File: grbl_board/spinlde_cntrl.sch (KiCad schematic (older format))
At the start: 11 parts

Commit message: spindle control stage
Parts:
- removed C?: 100n, symbol Device:C
- removed U?: LMV321, symbol Amplifier_Operational:LMV321
- added C? (x2): 100n, symbol Device:C
- added C? (x2): 220p, symbol Device:C
- added C?: 10u, symbol Device:C
- added C?: 6.8n, symbol Device:C
- added C?: 100u, symbol Device:C
- added D? (x2): 1N4148, Diode_THT:D_DO-35_SOD27_P7.62mm_Horizontal, symbol Diode:1N4148
- added D?: SS2150-LTP, symbol Device:D_Schottky
- added D? (x2): BZX84Cxx, Diode_SMD:D_SOT-23_ANK, symbol Diode:BZX84Cxx
- added J?: freq, symbol Connector:Screw_Terminal_01x02
- added J?: Spindle, symbol Connector:Screw_Terminal_01x02
- added L?: 33u, symbol Device:L
- added Q?: NDS7002A, symbol Device:Q_NMOS_GSD
- added Q?: Q_PMOS_GDS, symbol Device:Q_PMOS_GDS
- added Q? (x2): BSS127S, Package_TO_SOT_SMD:SOT-23, symbol Transistor_FET:BSS127S
- added R? (x2): 100, symbol Device:R
- added R? (x5): 10k, symbol Device:R
- added R?: 250, symbol Device:R
- added R?: 22, symbol Device:R
- added R? (x2): 5k, symbol Device:R
- added R? (x3): 4k, symbol Device:R
- added R?: 1k, symbol Device:R
- added R? (x3): 500, symbol Device:R
- added R? (x2): 1, symbol Device:R
- added R?: 47k, symbol Device:R
- added R?: 2.2k, symbol Device:R
- added R?: 200, symbol Device:R
- added U?: L7805, symbol Regulator_Linear:L7805
- added U?: OPA2192, symbol grbl_board:OPA2192
- added U? (x3): LMV358, symbol Amplifier_Operational:LMV358
- added U?: BD9G341EFJ, Package_SO:HTSOP-8-1EP_3.9x4.9mm_P1.27mm_EP2.4x3.2mm_ThermalVias, symbol Regulator_Switching:BD9G341EFJ
- added U? (x2): 6N137, Package_DIP:DIP-8_W7.62mm, symbol Isolator:6N137
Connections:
- net labels added: 12V, 1V_REF, 24V_VFD, GND_VFD, SPINDLE_DIR, SPINDLE_EN
- wire segments 32 -> 203
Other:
- moved on the sheet: C?, J?, R?, U?

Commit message: changed to matched resistor
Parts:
- removed R? (x2): 10k, symbol Device:R
- added RN? (x2): LT5400_10k, symbol Device:R_Pack04_Split
- Q?: value Q_PMOS_GDS -> IRF9Z24S
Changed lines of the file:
@@
 P 9350 4950
 F 0 "Q?" H 9555 4996 50  0000 L CNN
-F 1 "Q_PMOS_GDS" H 9555 4905 50  0000 L CNN
+F 1 "IRF9Z24S" H 9555 4905 50  0000 L CNN
 F 2 "" H 9550 5050 50  0001 C CNN
 F 3 "~" H 9350 4950 50  0001 C CNN
@@
 Wire Wire Line
 	7550 3050 7550 3150
-$Comp
-L Device:R R?
-U 1 1 62254479
-P 7550 2900
-F 0 "R?" H 7620 2946 50  0000 L CNN
-F 1 "10k" H 7620 2855 50  0000 L CNN
-F 2 "" V 7480 2900 50  0001 C CNN
-F 3 "~" H 7550 2900 50  0001 C CNN
-	1    7550 2900
-	1    0    0    -1
-$EndComp
 Wire Wire Line
 	8050 2650 8050 2700
@@
 Wire Wire Line
 	9450 4450 9450 4550
-$Comp
-L Device:R R?
-U 1 1 622497C7
-P 9450 4300
-F 0 "R?" H 9520 4346 50  0000 L CNN
-F 1 "10k" H 9520 4255 50  0000 L CNN
-F 2 "" V 9380 4300 50  0001 C CNN
-F 3 "~" H 9450 4300 50  0001 C CNN
-	1    9450 4300
-	1    0    0    -1
-$EndComp
 Wire Wire Line
 	9100 3800 9150 3800
@@
 Wire Wire Line
 	2300 6750 2950 6750
+$Comp
+L Device:R_Pack04_Split RN?
+U 1 1 6182439D
+P 9450 4300
+F 0 "RN?" H 9538 4346 50  0000 L CNN
+F 1 "LT5400_10k" H 9538 4255 50  0000 L CNN
+F 2 "" V 9370 4300 50  0001 C CNN
+F 3 "~" H 9450 4300 50  0001 C CNN
+	1    9450 4300
+	1    0    0    -1
+$EndComp
+$Comp
+L Device:R_Pack04_Split RN?
+U 2 1 61833B71
+P 7550 2900
+F 0 "RN?" H 7638 2946 50  0000 L CNN
+F 1 "LT5400_10k" H 7638 2855 50  0000 L CNN
+F 2 "" V 7470 2900 50  0001 C CNN
+F 3 "~" H 7550 2900 50  0001 C CNN
+	2    7550 2900
+	1    0    0    -1
+$EndComp
 $EndSCHEMATC

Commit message: added some footprint associations
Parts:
- removed Q?: NDS7002A, symbol Device:Q_NMOS_GSD
- added D46: LED, symbol Device:LED
- added Q3: ZVN4306GTA, Package_TO_SOT_SMD:SOT-223-3_TabPin2, symbol Device:Q_NMOS_GDS
- added R50: 270, Resistor_SMD:R_0805_2012Metric_Pad1.15x1.40mm_HandSolder, symbol Device:R
- C26: renamed from C?; footprint (none) -> Capacitor_SMD:C_0402_1005Metric_Pad0.74x0.62mm_HandSolder; Digikey Part No. (none) -> 1276-CL05B682KB5VPNCCT-ND
- C27, C28, C30, C33, C34: renamed from C?; footprint (none) -> Capacitor_SMD:C_0603_1608Metric_Pad1.05x0.95mm_HandSolder; Digikey Part No. (none) -> 1276-1941-1-ND
- C31, C32: renamed from C?; footprint (none) -> Capacitor_SMD:C_0402_1005Metric_Pad0.74x0.62mm_HandSolder; Digikey Part No. (none) -> CL05C221JB5NNNC
- J14, J15, J16: renamed from J?; footprint (none) -> Connector_Phoenix_MC:PhoenixContact_MC_1,5_2-G-3.81_1x02_P3.81mm_Horizontal; Digikey Part No. (none) -> ED2808-ND
- L4: renamed from L?; footprint (none) -> Inductor_SMD:L_Vishay_IHLP-4040; Digikey Part No. (none) -> 541-2273-1-ND
- Q1, Q2: renamed from Q?; Digikey Part No. (none) -> BSS127S-7DICT-ND
- Q4: renamed from Q?; value IRF9Z24S -> IRF9Z24SPBF; footprint (none) -> Package_TO_SOT_SMD:TO-263-3_TabPin2; Digikey Part No. (none) -> IRF9Z24SPBF-ND
- R25, R26, R27: renamed from R?; value 500 -> 270; footprint (none) -> Resistor_SMD:R_0805_2012Metric_Pad1.15x1.40mm_HandSolder; Digikey Part No. (none) -> YAG6172CT-ND
- R28: renamed from R?; value 1 -> 100k; footprint (none) -> Resistor_SMD:R_0603_1608Metric_Pad0.98x0.95mm_HandSolder; Digikey Part No. (none) -> 311-100KGRCT-ND
- R29: renamed from R?; value 1 -> 10k; footprint (none) -> Resistor_SMD:R_0805_2012Metric_Pad1.15x1.40mm_HandSolder; Digikey Part No. (none) -> 311-10KARCT-ND
- R30, R31, R32, R34, R35, R36, R39: renamed from R?; footprint (none) -> Resistor_SMD:R_0805_2012Metric_Pad1.15x1.40mm_HandSolder; Digikey Part No. (none) -> 311-10KARCT-ND
- R33: renamed from R?; footprint (none) -> Resistor_SMD:R_0805_2012Metric_Pad1.15x1.40mm_HandSolder; Digikey Part No. (none) -> 311-47KARCT-ND
- R37: renamed from R?; footprint (none) -> Resistor_SMD:R_0603_1608Metric_Pad0.98x0.95mm_HandSolder; Digikey Part No. (none) -> 311-2.2KGRCT-ND
- R38: renamed from R?; footprint (none) -> Resistor_SMD:R_0603_1608Metric_Pad0.98x0.95mm_HandSolder; Digikey Part No. (none) -> 311-200GRCT-ND
- R40: renamed from R?; value 4k -> 12k; footprint (none) -> Resistor_SMD:R_0805_2012Metric_Pad1.15x1.40mm_HandSolder; Digikey Part No. (none) -> 311-12KARCT-ND
- R41: renamed from R?; value 1k -> 3k; footprint (none) -> Resistor_SMD:R_0603_1608Metric_Pad0.98x0.95mm_HandSolder; Digikey Part No. (none) -> 311-3.0KGRCT-ND
- R42, R43: renamed from R?; value 5k -> 30k; footprint (none) -> Resistor_SMD:R_0603_1608Metric_Pad0.98x0.95mm_HandSolder; Digikey Part No. (none) -> 311-30KGRCT-ND
- R44, R45: renamed from R?; value 4k -> 24k; footprint (none) -> Resistor_SMD:R_0805_2012Metric_Pad1.15x1.40mm_HandSolder; Digikey Part No. (none) -> 311-24KARCT-ND
- R47, R48: renamed from R?; footprint (none) -> Resistor_SMD:R_0603_1608Metric_Pad0.98x0.95mm_HandSolder; Digikey Part No. (none) -> 311-100GRCT-ND
- R49: renamed from R?; footprint (none) -> Resistor_SMD:R_0805_2012Metric_Pad1.15x1.40mm_HandSolder; Digikey Part No. (none) -> 13-RT0805BRD0722RLCT-ND
- RN1: renamed from RN?; footprint (none) -> Package_SO:TSSOP-8_3x3mm_P0.65mm; Digikey Part No. (none) -> 505-LT5400ACMS8E-1#PBF-ND
- gave numbers to parts that had none: 15
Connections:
- wire segments 203 -> 205

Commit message: complete footprint associations
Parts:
- removed C25: 10u, symbol Device:C
- removed C29: 100u, symbol Device:C
- added C25: 10u, Capacitor_THT:CP_Radial_D8.0mm_P3.50mm, symbol Device:CP
- added C29: 100u, Capacitor_THT:CP_Radial_D8.0mm_P3.50mm, symbol Device:CP
- D43: footprint (none) -> Diode_SMD:D_SMA_Handsoldering; Digikey Part No. (none) -> SS2150-LTPMSCT-ND
- D46: footprint (none) -> LED_SMD:LED_1206_3216Metric_Pad1.42x1.75mm_HandSolder; Digikey Part No. (none) -> 404-1046-1-ND
- R46: footprint (none) -> Resistor_SMD:R_0603_1608Metric_Pad0.98x0.95mm_HandSolder; Digikey Part No. (none) -> 13-RT0603BRE07250RLCT-ND
- U18, U19, U20: Digikey Part No. (none) -> 6N137-X007TCT-ND
- U21: Digikey Part No. (none) -> BD9G341AEFJ-E2CT-ND
- U22: footprint (none) -> Package_SO:SOIC-8_3.9x4.9mm_P1.27mm; Digikey Part No. (none) -> LMV358DR2GOSCT-ND
- U23: footprint (none) -> Package_SO:TSSOP-8_3x3mm_P0.65mm; Digikey Part No. (none) -> 296-50480-1-ND
- U24: footprint (none) -> Package_TO_SOT_SMD:TO-263-2; Digikey Part No. (none) -> 497-1170-1-ND
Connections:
- net 12V: now also C29.1
- net 24V_VFD: now also C25.1
- net GND_VFD: now also C25.2, C29.2
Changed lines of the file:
@@
 F 0 "U22" H 6050 5867 50  0000 C CNN
 F 1 "LMV358" H 6050 5776 50  0000 C CNN
-F 2 "" H 6050 5500 50  0001 C CNN
-F 3 "http://www.ti.com/lit/ds/symlink/lmv324.pdf" H 6050 5500 50  0001 C CNN
+F 2 "Package_SO:SOIC-8_3.9x4.9mm_P1.27mm" H 6050 5500 50  0001 C CNN
+F 3 "https://www.onsemi.com/pdf/datasheet/lmv321-d.pdf" H 6050 5500 50  0001 C CNN
+F 4 "LMV358DR2GOSCT-ND" H 6050 5500 50  0001 C CNN "Digikey Part No."
 	1    6050 5500
 	1    0    0    -1
@@
 F 0 "U22" H 6150 4167 50  0000 C CNN
 F 1 "LMV358" H 6150 4076 50  0000 C CNN
-F 2 "" H 6150 3800 50  0001 C CNN
-F 3 "http://www.ti.com/lit/ds/symlink/lmv324.pdf" H 6150 3800 50  0001 C CNN
+F 2 "Package_SO:SOIC-8_3.9x4.9mm_P1.27mm" H 6150 3800 50  0001 C CNN
+F 3 "https://www.onsemi.com/pdf/datasheet/lmv321-d.pdf" H 6150 3800 50  0001 C CNN
+F 4 "LMV358DR2GOSCT-ND" H 6150 3800 50  0001 C CNN "Digikey Part No."
 	2    6150 3800
 	1    0    0    -1
@@
 F 0 "U22" H 5908 2346 50  0000 L CNN
 F 1 "LMV358" H 5908 2255 50  0000 L CNN
-F 2 "" H 5950 2300 50  0001 C CNN
-F 3 "http://www.ti.com/lit/ds/symlink/lmv324.pdf" H 5950 2300 50  0001 C CNN
+F 2 "Package_SO:SOIC-8_3.9x4.9mm_P1.27mm" H 5950 2300 50  0001 C CNN
+F 3 "https://www.onsemi.com/pdf/datasheet/lmv321-d.pdf" H 5950 2300 50  0001 C CNN
+F 4 "LMV358DR2GOSCT-ND" H 5950 2300 50  0001 C CNN "Digikey Part No."
 	3    5950 2300
 	1    0    0    -1
@@
 F 0 "R46" H 7170 2946 50  0000 L CNN
 F 1 "250" H 7170 2855 50  0000 L CNN
-F 2 "" V 7030 2900 50  0001 C CNN
-F 3 "~" H 7100 2900 50  0001 C CNN
+F 2 "Resistor_SMD:R_0603_1608Metric_Pad0.98x0.95mm_HandSolder" V 7030 2900 50  0001 C CNN
+F 3 "https://www.yageo.com/upload/media/product/productsearch/datasheet/rchip/PYu-RT_1-to-0.01_RoHS_L_12.pdf" H 7100 2900 50  0001 C CNN
+F 4 "13-RT0603BRE07250RLCT-ND" H 7100 2900 50  0001 C CNN "Digikey Part No."
 	1    7100 2900
 	1    0    0    -1
@@
 F 0 "U23" H 8200 4800 50  0000 C CNN
 F 1 "OPA2192" H 8300 4700 50  0000 C CNN
-F 2 "" H 8050 4100 50  0001 C CNN
-F 3 "" H 8050 4100 50  0001 C CNN
+F 2 "Package_SO:TSSOP-8_3x3mm_P0.65mm" H 8050 4100 50  0001 C CNN
+F 3 "https://www.ti.com/general/docs/suppproductinfo.tsp?distId=10&gotoUrl=https%3A%2F%2Fwww.ti.com%2Flit%2Fgpn%2Fopa2192-q1" H 8050 4100 50  0001 C CNN
+F 4 "296-50480-1-ND" H 8050 4100 50  0001 C CNN "Digikey Part No."
 	1    8050 4100
 	1    0    0    -1
@@
 F 1 "6N137" H 2050 4176 50  0000 C CNN
 F 2 "Package_DIP:DIP-8_W7.62mm" H 2050 3300 50  0001 C CNN
-F 3 "https://docs.broadcom.com/docs/AV02-0940EN" H 1200 4350 50  0001 C CNN
+F 3 "https://www.vishay.com/docs/84732/6n137.pdf" H 1200 4350 50  0001 C CNN
+F 4 "6N137-X007TCT-ND" H 2050 3800 50  0001 C CNN "Digikey Part No."
 	1    2050 3800
 	1    0    0    -1
@@
 Text Label 1700 1150 1    50   ~ 0
 24V_VFD
-Connection ~ 1700 1850
-Wire Wire Line
-	1250 1850 1700 1850
-Wire Wire Line
-	1250 1550 1250 1850
 Wire Wire Line
 	1150 1450 1700 1450
@@
 F 0 "D43" V 3854 2580 50  0000 L CNN
 F 1 "SS2150-LTP" V 3945 2580 50  0000 L CNN
-F 2 "" H 3900 2500 50  0001 C CNN
-F 3 "~" H 3900 2500 50  0001 C CNN
+F 2 "Diode_SMD:D_SMA_Handsoldering" H 3900 2500 50  0001 C CNN
+F 3 "https://www.mccsemi.com/pdf/Products/SS22-L-SS220-L(DO-214AC).pdf" H 3900 2500 50  0001 C CNN
+F 4 "SS2150-LTPMSCT-ND" H 3900 2500 50  0001 C CNN "Digikey Part No."
 	1    3900 2500
 	0    1    1    0
@@
 Wire Wire Line
 	4500 1500 4500 1450
-$Comp
-L Device:C C?
-U 1 1 62356FB4
-P 4500 1650
-AR Path="/619755E7/62356FB4" Ref="C?"  Part="1"
-AR Path="/61DA711F/62356FB4" Ref="C29"  Part="1"
-F 0 "C29" H 4615 1696 50  0000 L CNN
-F 1 "100u" H 4615 1605 50  0000 L CNN
-F 2 "" H 4538 1500 50  0001 C CNN
-F 3 "~" H 4500 1650 50  0001 C CNN
-	1    4500 1650
-	1    0    0    -1
-$EndComp
 Wire Wire Line
 	4050 1450 4500 1450
@@
 $EndComp
 Wire Wire Line
-	1700 1950 1700 1850
-Wire Wire Line
 	1700 1450 2150 1450
 Connection ~ 1700 1450
 Wire Wire Line
 	1700 1550 1700 1450
-$Comp
-L Device:C C?
-U 1 1 62356F5F
-P 1700 1700
-AR Path="/619755E7/62356F5F" Ref="C?"  Part="1"
-AR Path="/61DA711F/62356F5F" Ref="C25"  Part="1"
-F 0 "C25" H 1815 1746 50  0000 L CNN
-F 1 "10u" H 1815 1655 50  0000 L CNN
-F 2 "" H 1738 1550 50  0001 C CNN
-F 3 "~" H 1700 1700 50  0001 C CNN
-	1    1700 1700
-	1    0    0    -1
-$EndComp
 Wire Wire Line
 	2150 2150 2150 2050
@@
 F 2 "Package_SO:HTSOP-8-1EP_3.9x4.9mm_P1.27mm_EP2.4x3.2mm_ThermalVias" H 3050 1300 50  0001 L CNN
 F 3 "https://media.digikey.com/pdf/Data%20Sheets/Rohm%20PDFs/BD9G341EFJ.pdf" H 2950 1750 50  0001 C CNN
+F 4 "BD9G341AEFJ-E2CT-ND" H 2950 1750 50  0001 C CNN "Digikey Part No."
 	1    2950 1750
 	1    0    0    -1
@@
 F 0 "U24" H 9650 2192 50  0000 C CNN
 F 1 "L7805" H 9650 2101 50  0000 C CNN
-F 2 "" H 9675 1800 50  0001 L CIN
+F 2 "Package_TO_SOT_SMD:TO-263-2" H 9675 1800 50  0001 L CIN
 F 3 "http://www.st.com/content/ccc/resource/technical/document/datasheet/41/4f/b3/b0/12/d4/47/88/CD00000444.pdf/files/CD00000444.pdf/jcr:content/translations/en.CD00000444.pdf" H 9650 1900 50  0001 C CNN
+F 4 "497-1170-1-ND" H 9650 1950 50  0001 C CNN "Digikey Part No."
 	1    9650 1950
 	1    0    0    -1
@@
 F 1 "6N137" H 2000 5876 50  0000 C CNN
 F 2 "Package_DIP:DIP-8_W7.62mm" H 2000 5000 50  0001 C CNN
-F 3 "https://docs.broadcom.com/docs/AV02-0940EN" H 1150 6050 50  0001 C CNN
+F 3 "https://www.vishay.com/docs/84732/6n137.pdf" H 1150 6050 50  0001 C CNN
+F 4 "6N137-X007TCT-ND" H 2000 5500 50  0001 C CNN "Digikey Part No."
 	1    2000 5500
 	1    0    0    -1
@@
 F 1 "6N137" H 2000 7126 50  0000 C CNN
 F 2 "Package_DIP:DIP-8_W7.62mm" H 2000 6250 50  0001 C CNN
-F 3 "https://docs.broadcom.com/docs/AV02-0940EN" H 1150 7300 50  0001 C CNN
+F 3 "https://www.vishay.com/docs/84732/6n137.pdf" H 1150 7300 50  0001 C CNN
+F 4 "6N137-X007TCT-ND" H 2000 6750 50  0001 C CNN "Digikey Part No."
 	1    2000 6750
 	1    0    0    -1
@@
 F 0 "D46" V 10647 3730 50  0000 L CNN
 F 1 "LED" V 10738 3730 50  0000 L CNN
-F 2 "" H 10700 3650 50  0001 C CNN
-F 3 "~" H 10700 3650 50  0001 C CNN
+F 2 "LED_SMD:LED_1206_3216Metric_Pad1.42x1.75mm_HandSolder" H 10700 3650 50  0001 C CNN
+F 3 "https://media.digikey.com/pdf/Data%20Sheets/Stanley%20Electric%20PDFs/1101W_Series.pdf" H 10700 3650 50  0001 C CNN
+F 4 "404-1046-1-ND" H 10700 3650 50  0001 C CNN "Digikey Part No."
 	1    10700 3650
 	0    -1   -1   0
@@
 Wire Wire Line
 	10700 3050 10700 3100
+$Comp
+L Device:CP C?
+U 1 1 61B273C0
+P 4500 1650
+AR Path="/619755E7/61B273C0" Ref="C?"  Part="1"
+AR Path="/61DA711F/61B273C0" Ref="C29"  Part="1"
+F 0 "C29" H 4618 1696 50  0000 L CNN
+F 1 "100u" H 4618 1605 50  0000 L CNN
+F 2 "Capacitor_THT:CP_Radial_D8.0mm_P3.50mm" H 4538 1500 50  0001 C CNN
+F 3 "https://www.tdk-electronics.tdk.com/inf/20/30/db/aec_2013/B41821_B43821.pdf" H 4500 1650 50  0001 C CNN
+F 4 "495-5986-ND" H 4500 1650 50  0001 C CNN "Digikey Part No."
+	1    4500 1650
+	1    0    0    -1
+$EndComp
+$Comp
+L Device:CP C?
+U 1 1 61B41092
+P 1700 1700
+AR Path="/619755E7/61B41092" Ref="C?"  Part="1"
+AR Path="/61DA711F/61B41092" Ref="C25"  Part="1"
+F 0 "C25" H 1818 1746 50  0000 L CNN
+F 1 "10u" H 1818 1655 50  0000 L CNN
+F 2 "Capacitor_THT:CP_Radial_D8.0mm_P3.50mm" H 1738 1550 50  0001 C CNN
+F 3 "https://www.tdk-electronics.tdk.com/inf/20/30/db/aec/B41866.pdf?ref_disty=digikey" H 1700 1700 50  0001 C CNN
+F 4 "495-75596-ND" H 1700 1700 50  0001 C CNN "Digikey Part No."
+	1    1700 1700
+	1    0    0    -1
+$EndComp
+Wire Wire Line
+	1700 1850 1700 1900
+Wire Wire Line
+	1700 1900 1250 1900
+Wire Wire Line
+	1250 1550 1250 1900
+Connection ~ 1700 1900
+Wire Wire Line
+	1700 1900 1700 1950
 $EndSCHEMATC

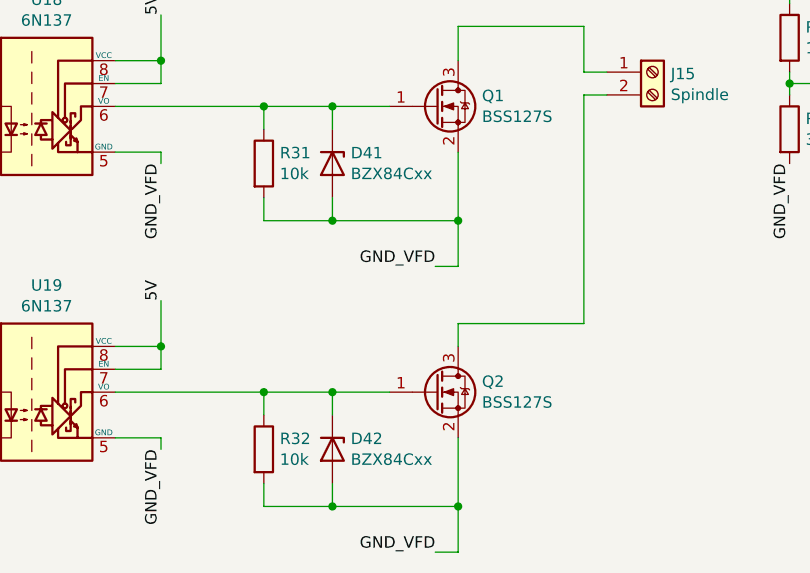
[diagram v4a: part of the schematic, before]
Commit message: fixed mismatch for 6n137
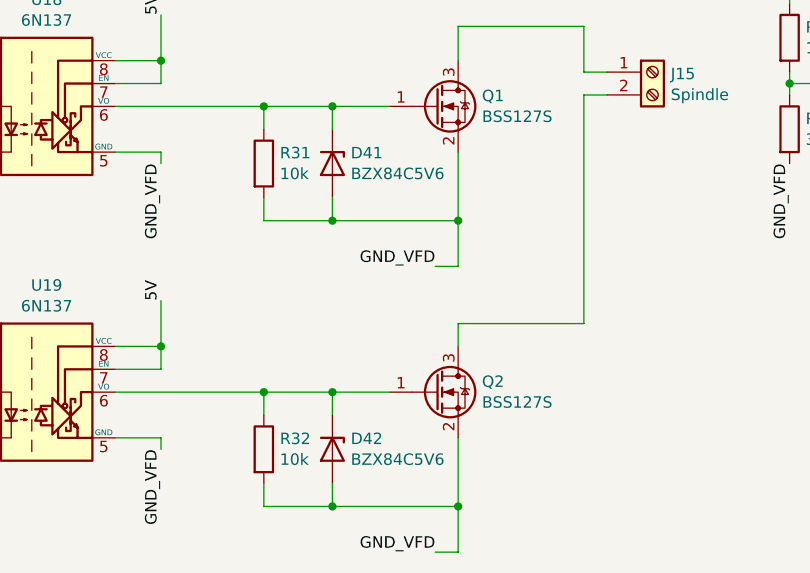
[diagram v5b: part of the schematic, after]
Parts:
- D41, D42: value BZX84Cxx -> BZX84C5V6; Digikey Part No. (none) -> 1514-BZX84C5V6TRPBFREECT-ND
- D44, D45: Digikey Part No. (none) -> 1N4148FS-ND
- U18, U19, U20: footprint Package_DIP:DIP-8_W7.62mm -> Package_DIP:DIP-8_W7.62mm_Socket; Digikey Part No. 6N137-X007TCT-ND -> 6N137IS-ND
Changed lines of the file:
@@
 F 2 "Diode_THT:D_DO-35_SOD27_P7.62mm_Horizontal" H 8500 5225 50  0001 C CNN
 F 3 "https://assets.nexperia.com/documents/data-sheet/1N4148_1N4448.pdf" H 8500 5400 50  0001 C CNN
+F 4 "1N4148FS-ND" H 8500 5400 50  0001 C CNN "Digikey Part No."
 	1    8500 5400
 	0    1    1    0
@@
 F 2 "Diode_THT:D_DO-35_SOD27_P7.62mm_Horizontal" H 8500 4875 50  0001 C CNN
 F 3 "https://assets.nexperia.com/documents/data-sheet/1N4148_1N4448.pdf" H 8500 5050 50  0001 C CNN
+F 4 "1N4148FS-ND" H 8500 5050 50  0001 C CNN "Digikey Part No."
 	1    8500 5050
 	0    1    1    0
@@
 F 0 "U20" H 2050 4267 50  0000 C CNN
 F 1 "6N137" H 2050 4176 50  0000 C CNN
-F 2 "Package_DIP:DIP-8_W7.62mm" H 2050 3300 50  0001 C CNN
-F 3 "https://www.vishay.com/docs/84732/6n137.pdf" H 1200 4350 50  0001 C CNN
-F 4 "6N137-X007TCT-ND" H 2050 3800 50  0001 C CNN "Digikey Part No."
+F 2 "Package_DIP:DIP-8_W7.62mm_Socket" H 2050 3300 50  0001 C CNN
+F 3 "http://isocom.com/wp-content/uploads/2017/10/DD93209-6N137_ICPL2601_2611-280917.pdf" H 1200 4350 50  0001 C CNN
+F 4 "6N137IS-ND" H 2050 3800 50  0001 C CNN "Digikey Part No."
 	1    2050 3800
 	1    0    0    -1
@@
 AR Path="/61DA711F/6256DA44" Ref="D41"  Part="1"
 F 0 "D41" V 3204 5830 50  0000 L CNN
-F 1 "BZX84Cxx" V 3295 5830 50  0000 L CNN
+F 1 "BZX84C5V6" V 3295 5830 50  0000 L CNN
 F 2 "Diode_SMD:D_SOT-23_ANK" H 3250 5575 50  0001 C CNN
 F 3 "https://diotec.com/tl_files/diotec/files/pdf/datasheets/bzx84c2v4.pdf" H 3250 5750 50  0001 C CNN
+F 4 "1514-BZX84C5V6TRPBFREECT-ND" H 3250 5750 50  0001 C CNN "Digikey Part No."
 	1    3250 5750
 	0    1    1    0
@@
 AR Path="/61DA711F/62579E21" Ref="D42"  Part="1"
 F 0 "D42" V 3204 7080 50  0000 L CNN
-F 1 "BZX84Cxx" V 3295 7080 50  0000 L CNN
+F 1 "BZX84C5V6" V 3295 7080 50  0000 L CNN
 F 2 "Diode_SMD:D_SOT-23_ANK" H 3250 6825 50  0001 C CNN
 F 3 "https://diotec.com/tl_files/diotec/files/pdf/datasheets/bzx84c2v4.pdf" H 3250 7000 50  0001 C CNN
+F 4 "1514-BZX84C5V6TRPBFREECT-ND" H 3250 7000 50  0001 C CNN "Digikey Part No."
 	1    3250 7000
 	0    1    1    0
@@
 F 0 "U18" H 2000 5967 50  0000 C CNN
 F 1 "6N137" H 2000 5876 50  0000 C CNN
-F 2 "Package_DIP:DIP-8_W7.62mm" H 2000 5000 50  0001 C CNN
-F 3 "https://www.vishay.com/docs/84732/6n137.pdf" H 1150 6050 50  0001 C CNN
-F 4 "6N137-X007TCT-ND" H 2000 5500 50  0001 C CNN "Digikey Part No."
+F 2 "Package_DIP:DIP-8_W7.62mm_Socket" H 2000 5000 50  0001 C CNN
+F 3 "http://isocom.com/wp-content/uploads/2017/10/DD93209-6N137_ICPL2601_2611-280917.pdf" H 1150 6050 50  0001 C CNN
+F 4 "6N137IS-ND" H 2000 5500 50  0001 C CNN "Digikey Part No."
 	1    2000 5500
 	1    0    0    -1
@@
 F 0 "U19" H 2000 7217 50  0000 C CNN
 F 1 "6N137" H 2000 7126 50  0000 C CNN
-F 2 "Package_DIP:DIP-8_W7.62mm" H 2000 6250 50  0001 C CNN
-F 3 "https://www.vishay.com/docs/84732/6n137.pdf" H 1150 7300 50  0001 C CNN
-F 4 "6N137-X007TCT-ND" H 2000 6750 50  0001 C CNN "Digikey Part No."
+F 2 "Package_DIP:DIP-8_W7.62mm_Socket" H 2000 6250 50  0001 C CNN
+F 3 "http://isocom.com/wp-content/uploads/2017/10/DD93209-6N137_ICPL2601_2611-280917.pdf" H 1150 7300 50  0001 C CNN
+F 4 "6N137IS-ND" H 2000 6750 50  0001 C CNN "Digikey Part No."
 	1    2000 6750
 	1    0    0    -1

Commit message: routing done
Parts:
- renumbered D41 to D38, D42 to D39, D43 to D40, D44 to D41, D45 to D42, D46 to D43

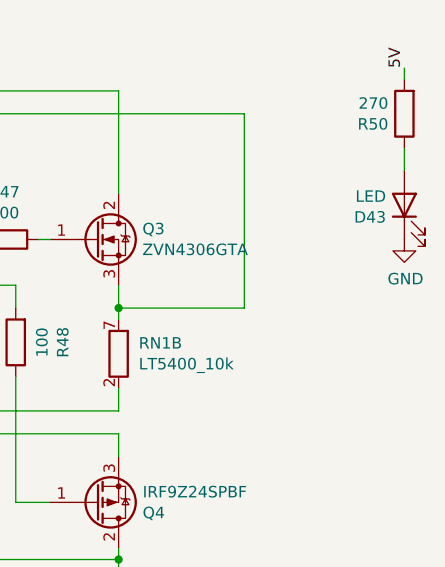
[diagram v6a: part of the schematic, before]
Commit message: added usb 3d model and fixed footprint associations
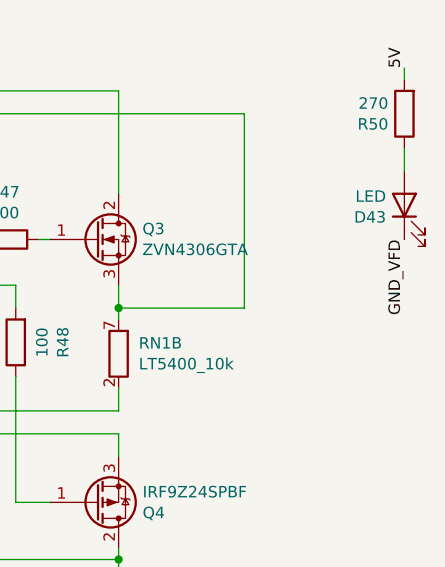
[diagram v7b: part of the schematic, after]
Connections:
- net GND: no longer D43.1 (K)
- net GND_VFD: now also D43.1 (K)
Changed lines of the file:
@@
 	1700 1900 1700 1950
-$Comp
-L power:GND #PWR?
-U 1 1 619C265E
-P 10700 3800
-AR Path="/61764E0B/619C265E" Ref="#PWR?"  Part="1"
-AR Path="/619755E7/619C265E" Ref="#PWR?"  Part="1"
-AR Path="/61DA711F/619C265E" Ref="#PWR077"  Part="1"
-F 0 "#PWR077" H 10700 3550 50  0001 C CNN
-F 1 "GND" H 10705 3627 50  0000 C CNN
-F 2 "" H 10700 3800 50  0001 C CNN
-F 3 "" H 10700 3800 50  0001 C CNN
-	1    10700 3800
-	1    0    0    -1
-$EndComp
 $Comp
 L Device:CP C?
@@
 	0    1    1    0
 $EndComp
+Text Label 10700 3800 3    50   ~ 0
+GND_VFD
 $EndSCHEMATC
